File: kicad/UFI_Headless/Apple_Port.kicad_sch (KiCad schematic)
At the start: 16 parts, among them J14 DISK_II, J15 APPLE_EN2, U16 SN74AHCT244PWR, U17 74LVC2G17GW, U18 ICL7662EBA+T

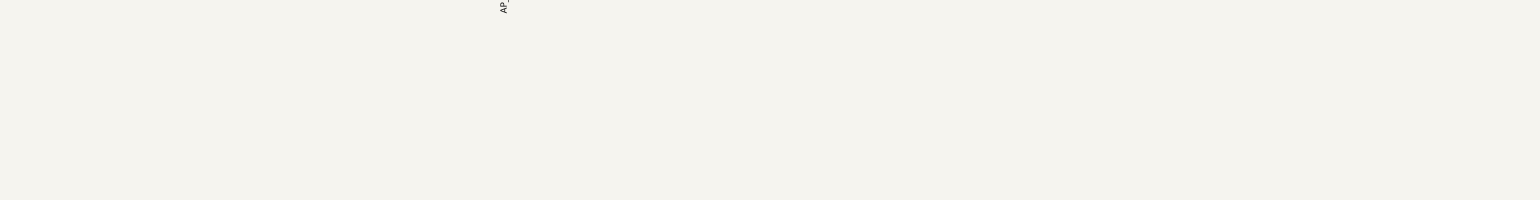
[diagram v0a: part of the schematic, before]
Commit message: v0.7: internal USB 2.0 header J16, PC PSU input J17 (F4, D17), 5V source jumper J18, Disk II sync sensor input J19; DRC 0, parity 0, fab data
route_try.py: own-net THT holes are no obstacle.
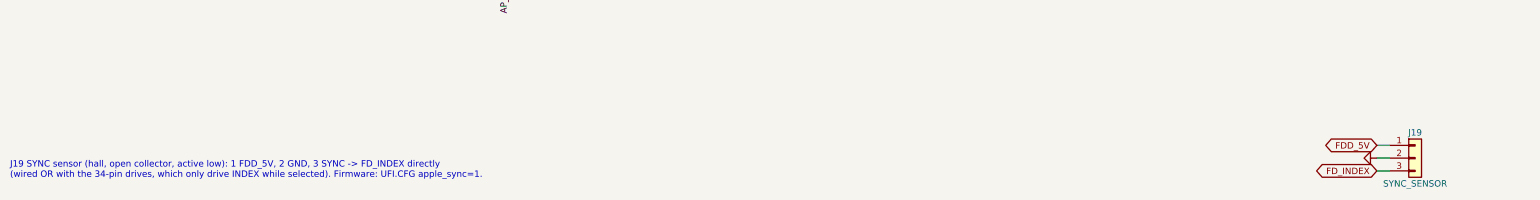
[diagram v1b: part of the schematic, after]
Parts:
- added J19: SYNC_SENSOR, Connector_PinHeader_2.54mm:PinHeader_1x03_P2.54mm_Vertical, symbol Connector_Generic:Conn_01x03
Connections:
- net FDD_5V: now also J19.1 (Pin_1)
- net GND: now also J19.2 (Pin_2)
- new net FD_INDEX: J19.3 (Pin_3)
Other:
- note added: "J19 SYNC sensor (hall, open collector, active low): 1 FDD_5V, 2 GND, 3 SYNC -> FD_INDEX directly (wired OR with the 34-pin drives, which only drive INDEX while selected). Firmware: UFI.CFG apple_sync=1."

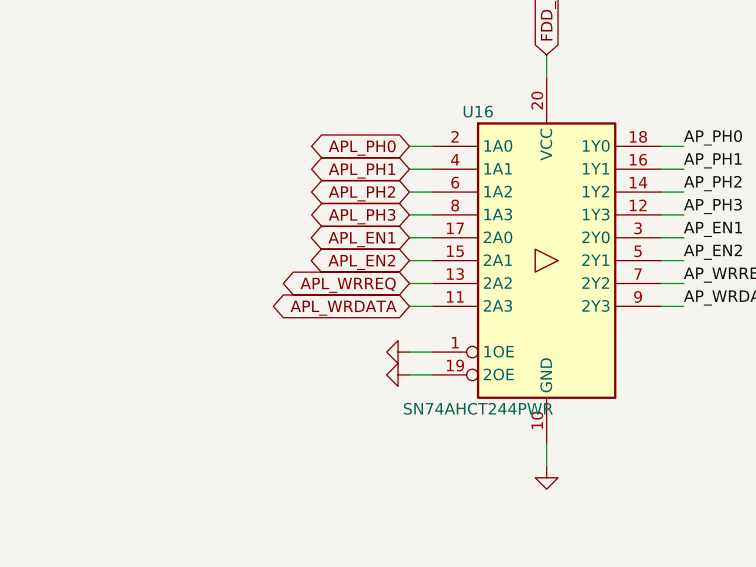
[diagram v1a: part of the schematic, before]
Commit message: KiCad v0.7 rework, stage A11a (owner's device-comparison list M1, M4, M6): write lock gates both write requests, terminations on FDD_5V, JP2 gone - Flux_Interface: U14 becomes a 74LVC1G32 (Diodes 74LVC1G32SE-7 C460530, SOT-353; was the 74LVC1G332 of A9b) forming the global net LOCK = WLOCK_HW or WLOCK_FW; new U30 74LVC2G32 (Nexperia 74LVC2G32DP,125 C548635, TSSOP-8; single-unit project symbol UFI_Headless:74LVC2G32 because the KiCad multi-unit symbol does not work with the MCP placement, pinout 1 1A 2 1B 3 2Y 4 GND 5 2A 6 2B 7 1Y 8 VCC from the datasheet family) gates FDD_WGATE -> FDD_WGATE_G (U7 pin 3, TP8) and APL_WRREQ -> APL_WRREQ_G (new global net to U16 2A2 on Apple_Port, the MCU-side pull-up RN10 stays on APL_WRREQ), C84 100 nF; both requests are active low, LOCK high forces them inactive, so the Apple write request no longer bypasses the lock (netlist: LOCK = U14.4 U30.2 U30.6, APL_WRREQ_G = U16.13 U30.3, FDD_WGATE_G = U7.3 U30.7 TP8.1). M4: R75-R91 (Flux_Interface) and R97-R99 (FDD_Connectors, same reason) pull up to FDD_5V instead of +5V, R92-R96 on the IEC bus stay at +5V. M6: JP2 with its GND symbol and labels removed, J6 pin 3 is GND. Note on the sheet. ERC over the whole project 0 errors / 0 warnings (build/erc.rpt). No firmware change (WLOCK_FW/WLOCK_HW semantics unchanged). PLAN.md A11a done, kicad README A11a row. PCB follows in B3.
Claude-Session: https://claude.ai/code/session_014MdzrcyXuayppPHbfEjUrw
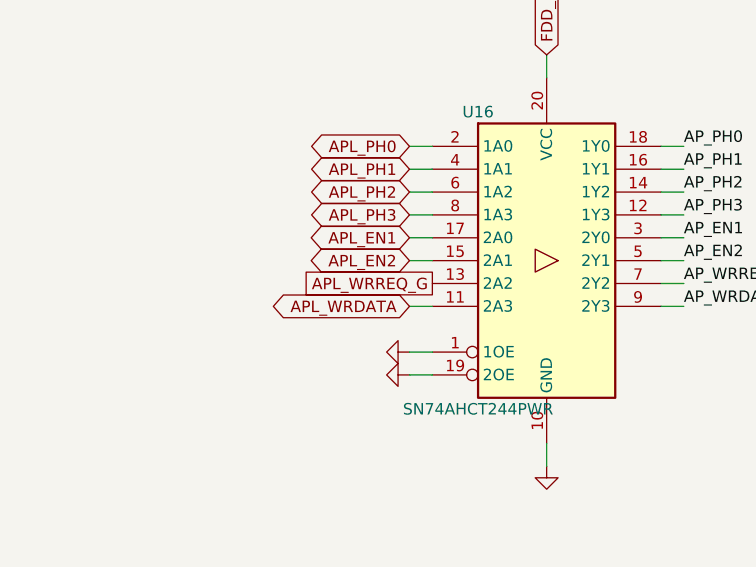
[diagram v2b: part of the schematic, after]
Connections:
- net APL_WRREQ: no longer U16.13 (2A2)
- new net APL_WRREQ_G: U16.13 (2A2)

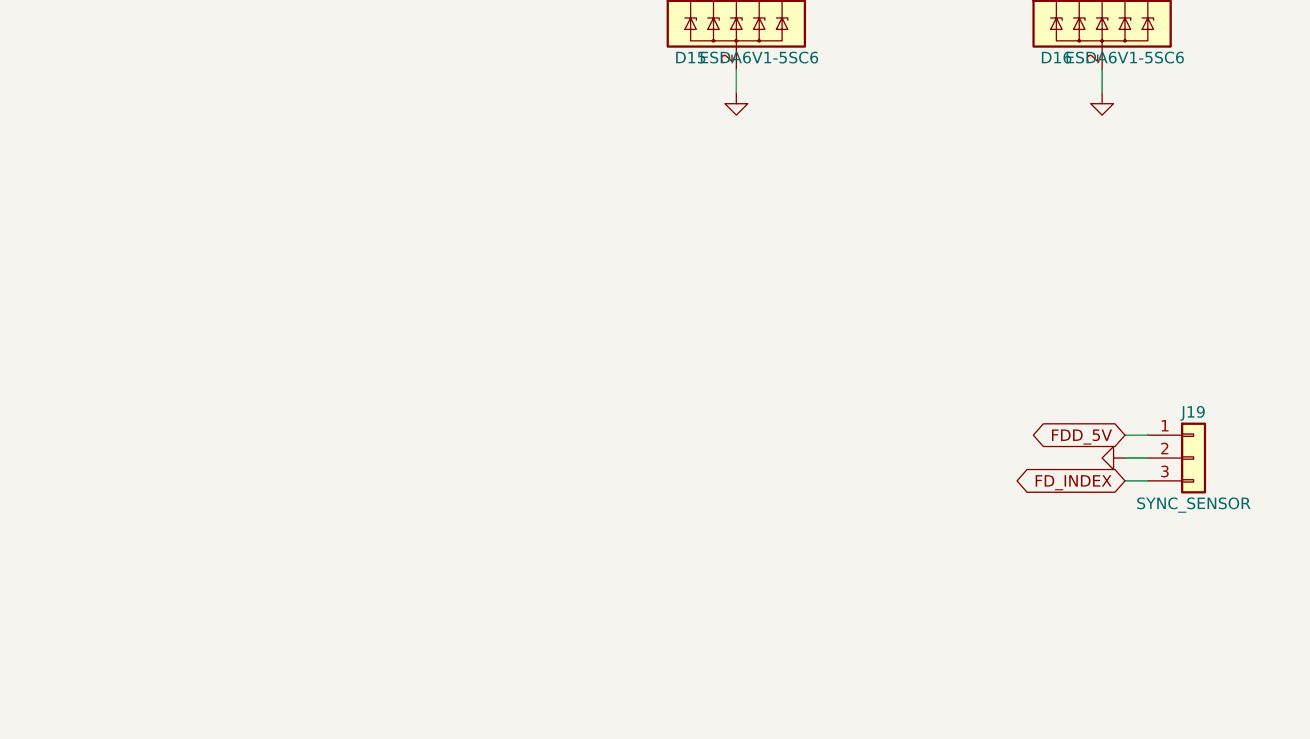
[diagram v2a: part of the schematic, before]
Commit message: KiCad v0.7 rework, stage A11d part 1 (owner's device-comparison list M5, S1-S4, S6; pins per docs/Timer_Zuteilung.md): sync sensor, J6 pin 2/4/33, rail voltage sense - Apple_Port: J19 pin 3 leaves the INDEX bus and becomes SYNC_5V with R165 10k to +3V3 and D30 PESD3V3L1BA, the new third Schmitt inverter U26 74LVC14AD (C133541, single-unit project symbol UFI_Headless:74LVC14_1U) turns it into SYNC -> PC6 (TIM8_CH1, AF3), also reads J6 pin 2 (FD_DENSITY) and pin 4 (FD_PIN4) back as FDD_PIN2_IN -> PD14 / FDD_PIN4_IN -> PD15 and reserves input 9 for the Mac !CSTOUT line of K1 (no-connect until A11d part 2), unused inputs on GND, C86 100 nF. FDD_Connectors: J6 pin 4 gets its own open-drain output Q12 BSS138DW (C154900, channel 1, gate FDD_PIN4 = PF14 with R158 100k, termination R159 1k to FDD_5V); J6 pin 33 moves from a fixed GND to the solder jumper JP7 (bridged to GND by default) whose third pad carries FLIPPY = PB5 through R156 2.2k with R157 2.2k to GND (2.2k instead of the planned 2.4k because 2.2k C4190 is already in the BOM). Power: R160/R161 10k/10k (FDD_5V / 2 -> V_FDD5 = PC4, ADC1 INP4) and R162/R163 33k/10k (FDD_12V / 4.3 -> V_FDD12 = PC5, ADC1 INP8). MCU_Core: no-connects on PC6, PD14, PD15, PF14, PB5, PC4, PC5, PB1 replaced by the global labels; PB0 (MAC_SEL) and PA8 (MAC_PWM) stay no-connect until the Mac header comes in part 2, PB1 = MAC_CSTOUT is already wired to U26. ERC over the whole project 0 errors / 0 warnings (build/erc.rpt). Firmware in the same commit: board.h/board_headless.c define PIN_SYNC, PIN_FDD_PIN2_IN, PIN_FDD_PIN4_IN, PIN_FDD_PIN4, PIN_FDD_PIN33, PIN_MAC_SEL, PIN_MAC_PWM, PIN_MAC_CSTOUT and ADC_CH_V_FDD5/V_FDD12 and initialise them as inputs or released (low) outputs; the TIM8 capture of SYNC, the rail-voltage limits (4.5 V / 10.8 V) and the protocol access follow in stage A10 (protocol doc: one hunk in the INDEX_SIM bullet - the sync sensor no longer drives the INDEX bus on v1.0, apple_sync has no effect there until A10). ARM build 0 wa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
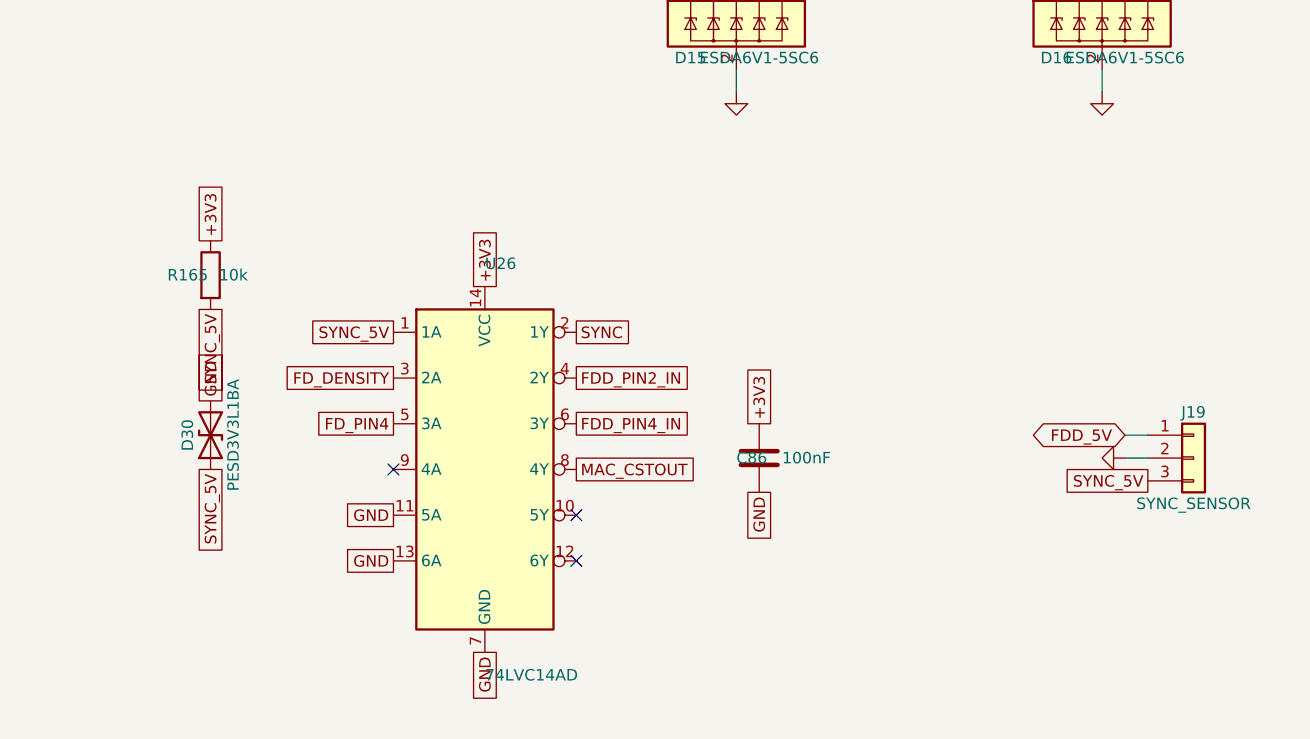
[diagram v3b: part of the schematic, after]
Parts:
- added C86: 100nF, Capacitor_SMD:C_0603_1608Metric, symbol Device:C
- added D30: PESD3V3L1BA, Diode_SMD:D_SOD-323, symbol Device:D_TVS
- added R165: 10k, Resistor_SMD:R_0603_1608Metric, symbol Device:R
- added U26: 74LVC14AD, Package_SO:SOIC-14_3.9x8.7mm_P1.27mm, symbol UFI_Headless:74LVC14_1U
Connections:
- net +3V3: now also C86.1, R165.1, U26.14 (VCC)
- net GND: now also C86.2, D30.2 (A2), U26.11 (5A), U26.13 (6A), U26.7 (GND)
- net FD_INDEX renamed SYNC_5V
- net SYNC_5V: now also D30.1 (A1), R165.2, U26.1 (1A)
- new net FDD_PIN2_IN: U26.4 (2Y)
- new net FDD_PIN4_IN: U26.6 (3Y)
- new net FD_DENSITY: U26.3 (2A)
- new net FD_PIN4: U26.5 (3A)
- new net MAC_CSTOUT: U26.8 (4Y)
- new net SYNC: U26.2 (1Y)
- no-connect marks 5 -> 8

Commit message: KiCad v0.7 rework, stage A11d part 2 (owner's list S5, S7, K1; owner decisions 2026-10-24: no D-sub on the board, pins 9/20 through solder jumpers default open, PWM line always on a Schmitt input, no fuse on the -12 V): Apple_Port: new Mac 3.5" port J23 (2x10 IDC, UFI_Headless:IDC-Header_2x10_P2.54mm_Vertical_UFI, C2977593) in the Apple internal 20-pin floppy pinout taken from the tashnotes connector document - 1/3/5/7 GND, 2/4/6/8 CA0/CA1/CA2/LSTRB on the Disk II phase nets AP_PH0-3, 10 !WRREQ (AP_WRREQ, gated by LOCK since A11a), 12 SEL = MAC_SEL_5V, 14 !ENBL = AP_EN2 (J15 removed), 16 RD = AP_RDDATA, 18 WR = AP_WRDATA, 11 FDD_5V, 13/15/17/19 FDD_12V, 9 = AP_M12V_J6 only through JP6 (open; 800K/FDHD drives output !EJECT there), 20 = CSTOUT_5V with R166 10k to FDD_5V, fed by the PWM driver only through JP5 (open; 800K/FDHD output !CSTOUT there) and always read back through U26 pin 9 -> MAC_CSTOUT = PB1; U27 SN74AHCT244PWR (C484743, FDD_5V, C87 100 nF) shifts MAC_SEL (PB0) and MAC_PWM (PA8, TIM1_CH1) to 5 V, unused inputs on GND and unused outputs no-connect; D31 ESDA6V1-5SC6 (C6650) on SEL and pin 20. S5: JP8 (bridged) between the ICL7662 output AP_M12V and J14 pin 9 (AP_M12V_J), no fuse - the pump limits to about 20 mA; U18 stays the ICL7662. Power: S7 USB shield J1 SH leaves GND and goes through R164 1M (C22935) parallel C85 4.7 nF (C53987) to GND (net USB_SHIELD). MCU_Core: PB0 = MAC_SEL and PA8 = MAC_PWM wired (no-connects removed). Notes on the Apple sheet. ERC over the whole project 0 errors / 0 warnings (build/erc.rpt). No firmware change in this part (the pins were defined and initialised released in part 1; the Mac drive driver SEL/PWM/CSTOUT and the 800K/FDHD GCR path are a firmware stage after A10), therefore no protocol change. PLAN.md (A11d complete, A11 done except the layout), kicad README (A11d-2 row). PCB follows in B3 (J23 placement with cable exit towards the enclosure socket).
Claude-Session: https://claude.ai/code/session_014MdzrcyXuayppPHbfEjU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
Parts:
- removed J15: APPLE_EN2, Connector_PinHeader_2.54mm:PinHeader_1x02_P2.54mm_Vertical, symbol Connector_Generic:Conn_01x02
- added C87: 100nF, Capacitor_SMD:C_0603_1608Metric, symbol Device:C
- added D31: ESDA6V1-5SC6, Package_TO_SOT_SMD:SOT-23-6, symbol Power_Protection:ESDA6V1-5SC6
- added J23: MAC_3.5_PORT, UFI_Headless:IDC-Header_2x10_P2.54mm_Vertical_UFI, symbol Connector_Generic:Conn_02x10_Odd_Even
- added JP5: MAC PWM (400K only), Jumper:SolderJumper-2_P1.3mm_Open_RoundedPad1.0x1.5mm, symbol Jumper:SolderJumper_2_Open
- added JP6: MAC -12V (400K only), Jumper:SolderJumper-2_P1.3mm_Open_RoundedPad1.0x1.5mm, symbol Jumper:SolderJumper_2_Open
- added JP8: DISK II -12V, Jumper:SolderJumper-2_P1.3mm_Bridged_RoundedPad1.0x1.5mm, symbol Jumper:SolderJumper_2_Bridged
- added R166: 10k, Resistor_SMD:R_0603_1608Metric, symbol Device:R
- added U27: SN74AHCT244PWR, Package_SO:TSSOP-20_4.4x6.5mm_P0.65mm, symbol 74xx:74AHCT244
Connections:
- net AP_EN2: now also J23.14 (Pin_14)
- net AP_M12V: now also JP6.1 (A), JP8.1 (A); no longer J14.9 (Pin_9)
- net AP_PH0: now also J23.2 (Pin_2)
- net AP_PH1: now also J23.4 (Pin_4)
- net AP_PH2: now also J23.6 (Pin_6)
- net AP_PH3: now also J23.8 (Pin_8)
- net AP_RDDATA: now also J23.16 (Pin_16)
- net AP_WRDATA: now also J23.18 (Pin_18)
- net AP_WRREQ: now also J23.10 (Pin_10)
- net FDD_12V: now also J23.13 (Pin_13), J23.15 (Pin_15), J23.17 (Pin_17), J23.19 (Pin_19)
- net FDD_5V: now also C87.1, J23.11 (Pin_11), R166.1, U27.20 (VCC)
- net GND: now also C87.2, D31.2 (GND), J23.1 (Pin_1), J23.3 (Pin_3), J23.5 (Pin_5), J23.7 (Pin_7), U27.1 (1OE), U27.10 (GND), U27.11 (2A3), U27.13 (2A2), U27.15 (2A1), U27.17 (2A0), U27.19 (2OE), U27.6 (1A2), U27.8 (1A3)
- net CSTOUT_5V: now reaches U26.9 (4A)
- net CSTOUT_5V: now also D31.3 (IO2), J23.20 (Pin_20), JP5.2 (B), R166.2
- new net AP_M12V_J: J14.9 (Pin_9), JP8.2 (B)
- new net AP_M12V_J6: J23.9 (Pin_9), JP6.2 (B)
- new net MAC_PWM: U27.4 (1A1)
- new net MAC_PWM_5V: JP5.1 (A), U27.16 (1Y1)
- new net MAC_SEL: U27.2 (1A0)
- new net MAC_SEL_5V: D31.1 (IO1), J23.12 (Pin_12), U27.18 (1Y0)
- no-connect marks 8 -> 16
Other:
- note added: "A11d (25.10.2026): K1 Mac 3.5" port J23 = Apple internal 20-pin floppy pinout (tashnotes connector document): 1/3/5/7 GND, 2 CA0, 4 CA1, 6 CA2, 8 LSTRB (= Disk II phases AP_PH0-3), 10 !WRREQ (gated by LOCK), 12 SEL (U27 <- PB0), 14 !ENBL (AP_EN2, J15 removed), 16 RD (AP_RDDATA, U17), 18 WR (AP_WRDATA), 11 +5V, 13/15/17/19 +12V. Pin 9: -12 V only through JP6 (open; 800K/FDHD drives output !EJECT t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"
